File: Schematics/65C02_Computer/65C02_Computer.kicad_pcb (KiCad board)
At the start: 2 copper layers, 203.2 x 149.9 mm, 67 parts, among them J1 CLK Jumper, J10 VIA2PB, J11 LCD Connector, J2 Optional UART Port, J3 USB_B_Micro, J4 USB_B, J5 Power Connector, J6 Mini-DIN-6, J7 Expansion port, J8 AVR-ISP-10, J9 VIA2PA, SW1 RESET, U1 74HC21, U10 ATtiny4313-PU, U11 65C22S, U12 65C22S, U2 74HC00, U3 74HC02, U4 NE555, U5 65C51N, U6 FT230XS, U7 65C02S, U8 28C256, U9 62256, X1 1MHz, X2 1.8432MHz

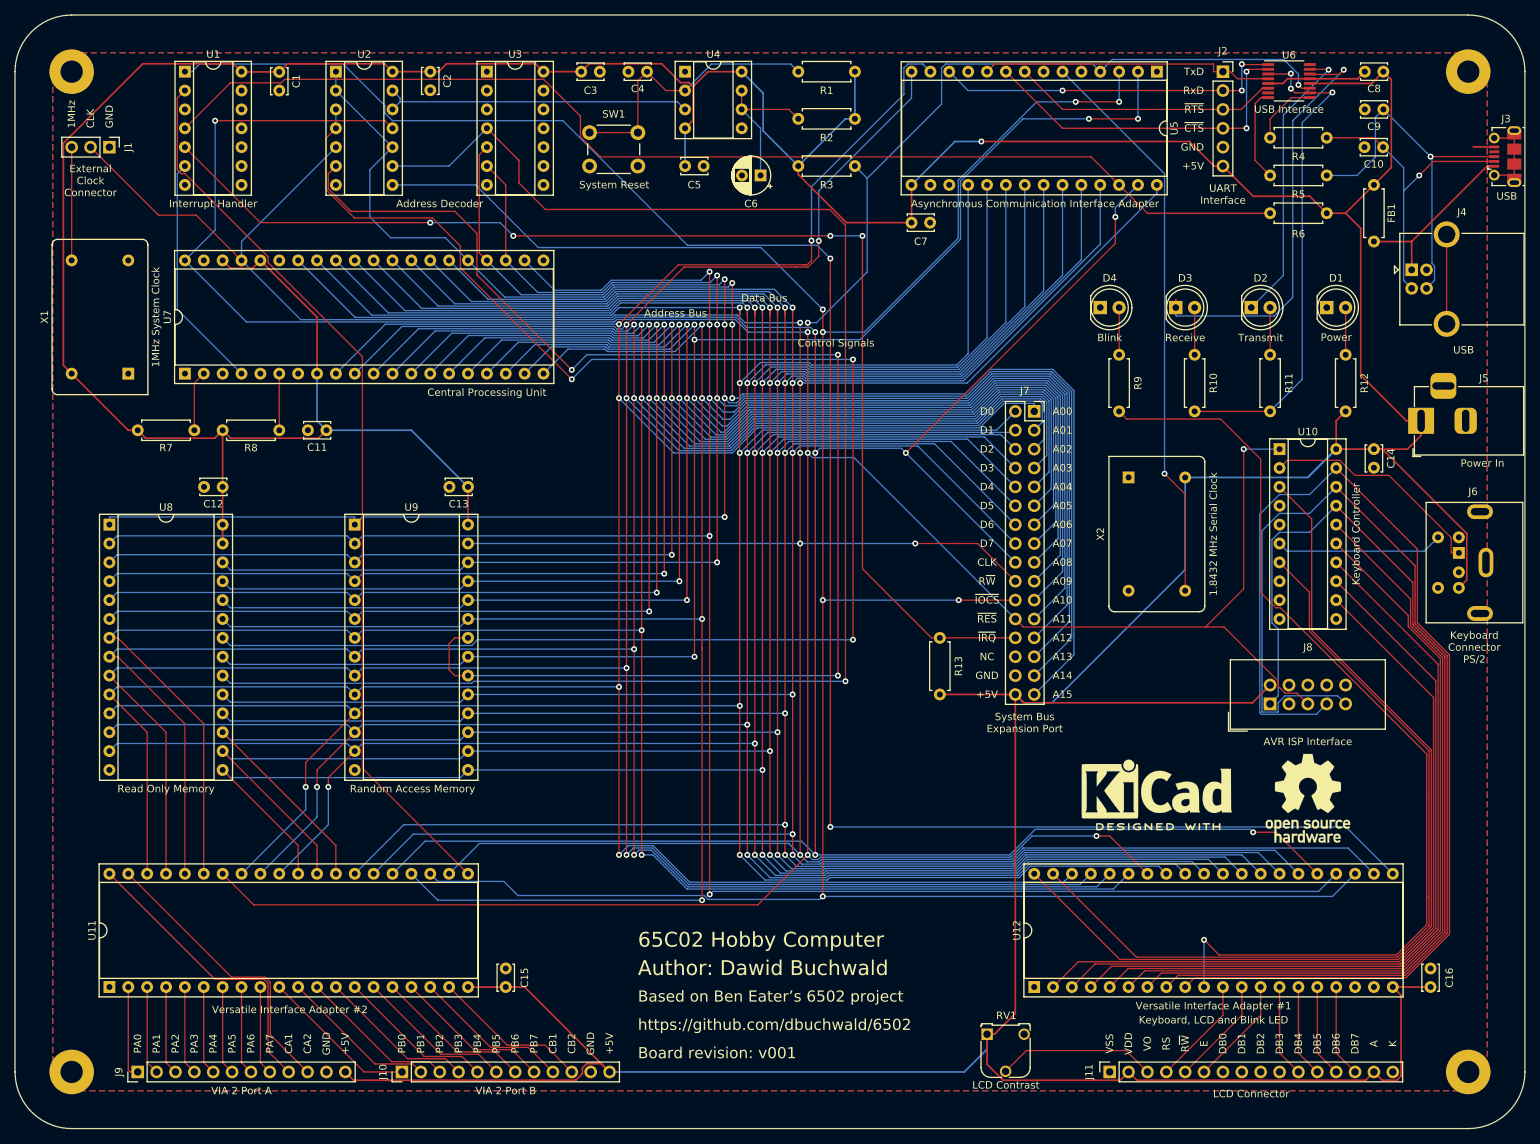
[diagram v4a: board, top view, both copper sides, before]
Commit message: Added one more Cap for stable power
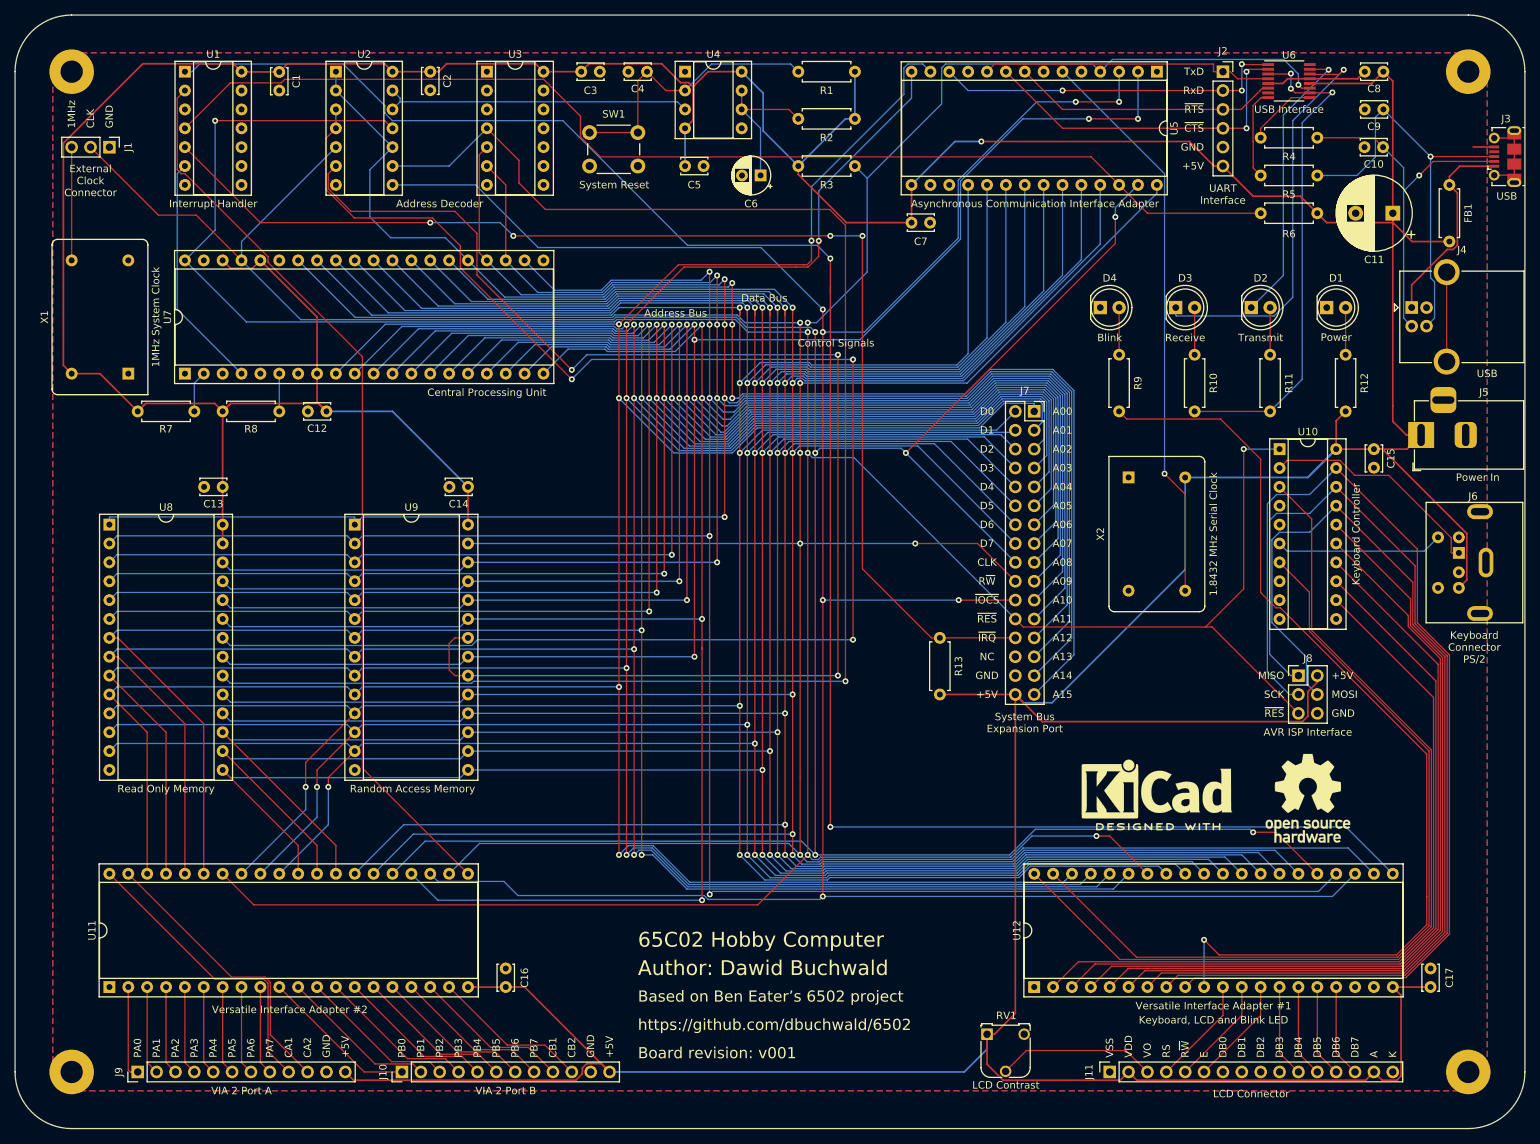
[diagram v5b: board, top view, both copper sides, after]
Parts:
- added C11: 1000uF, Capacitor_THT:CP_Radial_D10.0mm_P5.00mm, F.Cu at (203.2, 47.0)
- J8: footprint Connector_IDC:IDC-Header_2x05_P2.54mm_Vertical -> Connector_PinHeader_2.54mm:PinHeader_2x03_P2.54mm_Vertical
- moved FB1 12.7 mm to (210.8, 50.8), turned to 90 degrees
- moved J8 5.39 mm to (190.5, 109.2), turned to 0 degrees
- moved J4 5.08 mm to (205.7, 59.7)
- moved C12 2.54 mm to (59.7, 73.7)
- moved R7 2.54 mm to (41.9, 73.7)
- moved R8 2.54 mm to (53.3, 73.7)
- moved J5 1.90 mm to (207.0, 76.8)
- moved R4 1.27 mm to (185.4, 36.8)
- moved R5 1.27 mm to (185.4, 41.9)
- moved R6 1.27 mm to (193.0, 47.0)
- renumbered C11 to C12, C12 to C13, C13 to C14, C14 to C15, C15 to C16, C16 to C17
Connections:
- J8 pad 1: /6502 Peripherals/v1pa5 -> /6502 Peripherals/v1pa6
- J8 pad 3: Net-(J8-Pad3) -> /6502 Peripherals/v1pa7
- J8 pad 4: GND -> /6502 Peripherals/v1pa5
- U1 pad 10: (no net) -> GND
- U1 pad 12: (no net) -> GND
- U1 pad 13: (no net) -> GND
- U1 pad 8: (no net) -> Net-(U1-Pad8)
- U1 pad 9: (no net) -> GND
- U3 pad 1: (no net) -> Net-(U3-Pad1)
- U3 pad 10: (no net) -> Net-(U3-Pad10)
- U3 pad 11: (no net) -> GND
- U3 pad 12: (no net) -> GND
- U3 pad 13: (no net) -> Net-(U3-Pad13)
- U3 pad 2: (no net) -> GND
- U3 pad 3: (no net) -> GND
- U3 pad 8: (no net) -> GND
- U3 pad 9: (no net) -> GND
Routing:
- net +5V: track 851.1 -> 872.9 mm
- net /6502 Peripherals/v1pa6: track 157.2 -> 141.0 mm
- net /6502 Peripherals/v1pa7: track 156.8 -> 146.9 mm
- net PUSBD+: track 50.4 -> 57.0 mm
- net PUSBD-: track 42.6 -> 48.9 mm
- net Net-(FB1-Pad2): track 24.2 -> 27.7 mm
- net Net-(R8-Pad1): track 7.62 -> 5.08 mm
- net Net-(R7-Pad1): track 8.15 -> 5.61 mm
- net ~AIRQ: track 157.9 -> 156.6 mm
- net Net-(D3-Pad1): track 57.5 -> 56.4 mm
- net ~RES: track 547.8 -> 546.6 mm
- net USBD-: track 8.86 -> 9.39 mm
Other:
- board text added: "MISO"
- board text added: "MOSI"
- board text added: "SCK"

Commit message: PCB RC7
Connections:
- U3 pad 1: Net-(U3-Pad1) -> ~ROM_CS
- U3 pad 2: GND -> a14
- U3 pad 3: GND -> a13
- U3 pad 4: ~ROM_CS -> Net-(U3-Pad4)
- U3 pad 5: a14 -> GND
- U3 pad 6: a13 -> GND
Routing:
- net ~ROM_CS: track 216.2 -> 226.6 mm, vias 1 -> 3
- net a14: track 258.2 -> 265.8 mm
- net a13: track 239.1 -> 246.7 mm
